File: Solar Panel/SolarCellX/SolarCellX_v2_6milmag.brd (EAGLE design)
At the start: 100 x 82 mm, 17 parts

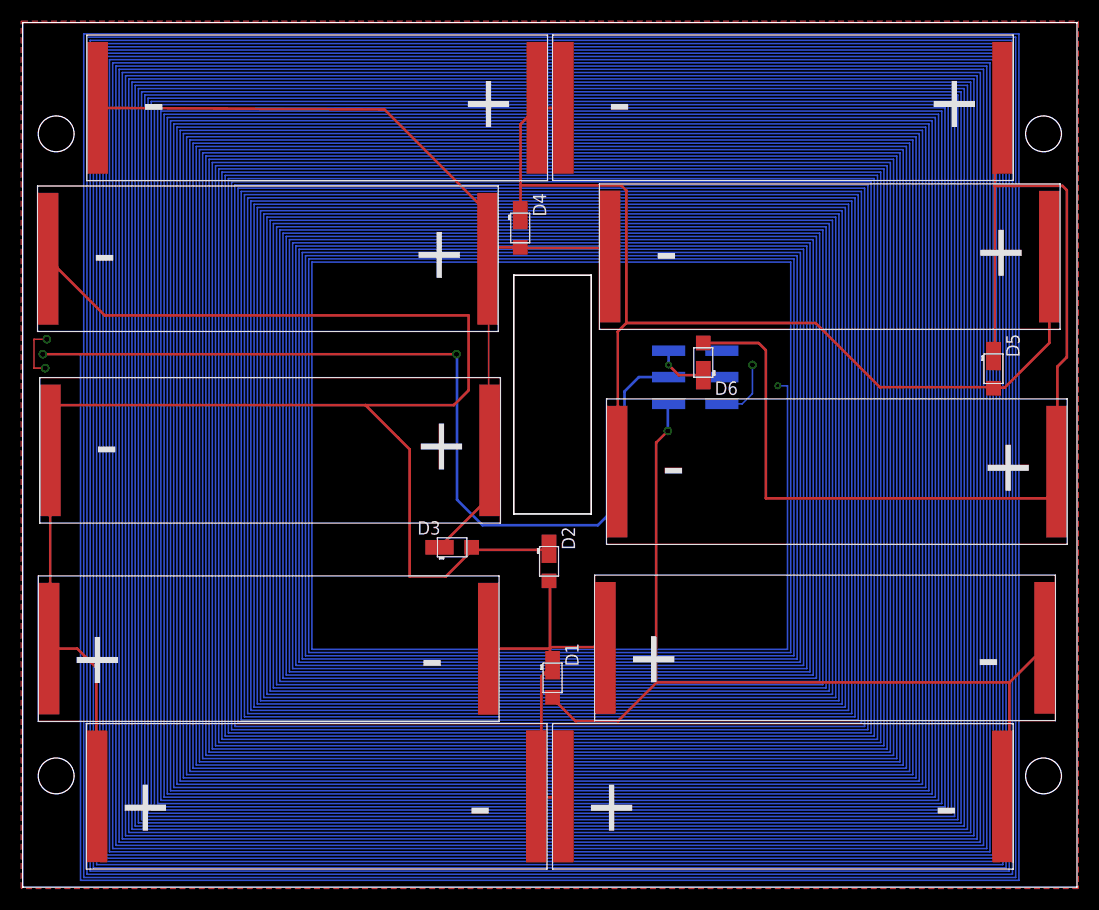
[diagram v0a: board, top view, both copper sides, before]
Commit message: Clearance fixes for X plus gerber generation
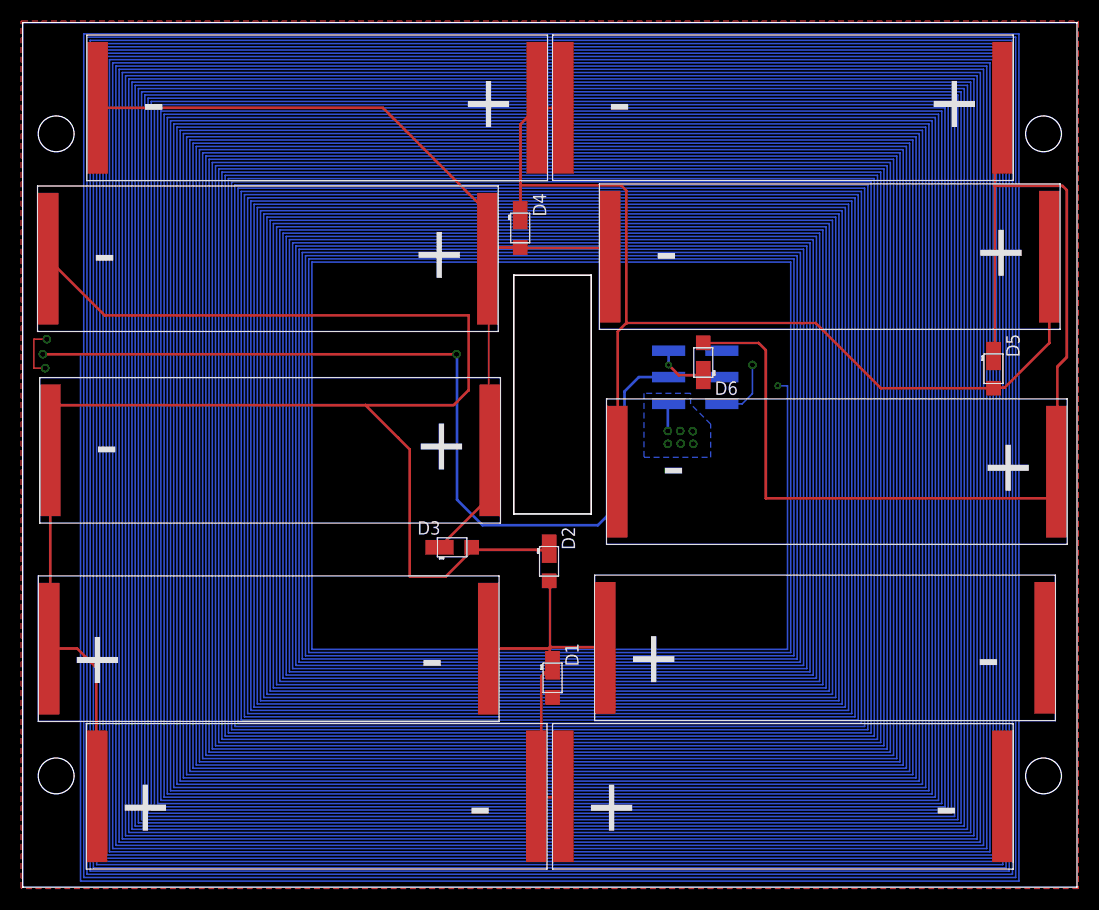
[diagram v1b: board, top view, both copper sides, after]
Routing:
- net GND: track 88.9 -> 2.65 mm, vias 1 -> 6
- added copper zone on layer 16, net GND
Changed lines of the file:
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@@
 <?xml version="1.0" encoding="utf-8"?>
 <!DOCTYPE eagle SYSTEM "eagle.dtd">
-<eagle version="9.3.0">
+<eagle version="9.2.2">
 <drawing>
 <settings>
@@
 <param name="mtCopper" value="0.035559375mm 0.01778125mm 0.0356mm 0.0356mm 0.0356mm 0.0356mm 0.0356mm 0.0356mm 0.0356mm 0.0356mm 0.0356mm 0.0356mm 0.0356mm 0.0356mm 0.01778125mm 0.035559375mm"/>
 <param name="mtIsolate" value="0.17018125mm 47mil 0.2007mm 0.1499mm 0.2007mm 0.1499mm 0.2007mm 0.1499mm 0.2007mm 0.1499mm 0.2007mm 0.1499mm 0.2007mm 0.1499mm 0.17018125mm"/>
-<param name="mdWireWire" value="5mil"/>
-<param name="mdWirePad" value="5mil"/>
-<param name="mdWireVia" value="5mil"/>
-<param name="mdPadPad" value="5mil"/>
-<param name="mdPadVia" value="5mil"/>
-<param name="mdViaVia" value="5mil"/>
-<param name="mdSmdPad" value="5mil"/>
-<param name="mdSmdVia" value="5mil"/>
-<param name="mdSmdSmd" value="5mil"/>
+<param name="mdWireWire" value="7mil"/>
+<param name="mdWirePad" value="7mil"/>
+<param name="mdWireVia" value="7mil"/>
+<param name="mdPadPad" value="7mil"/>
+<param name="mdPadVia" value="7mil"/>
+<param name="mdViaVia" value="7mil"/>
+<param name="mdSmdPad" value="6mil"/>
+<param name="mdSmdVia" value="6mil"/>
+<param name="mdSmdSmd" value="6mil"/>
 <param name="mdViaViaSameLayer" value="8mil"/>
 <param name="mnLayersViaInSmd" value="2"/>
@@
 <wire x1="61.191140625" y1="45.839" x2="61.191140625" y2="43.26381875" width="0.254" layer="16"/>
 <via x="61.191140625" y="43.26381875" extent="1-16" drill="0.5"/>
-<wire x1="61.191140625" y1="43.26381875" x2="60.0837" y2="42.156378125" width="0.254" layer="1"/>
-<wire x1="60.0837" y1="42.156378125" x2="60.0837" y2="19.4183" width="0.254" layer="1"/>
-<wire x1="52.4256" y1="15.748" x2="56.4642" y2="15.748" width="0.254" layer="1"/>
-<wire x1="50.292" y1="17.8816" x2="52.4256" y2="15.748" width="0.254" layer="1"/>
-<wire x1="50.292" y1="17.8816" x2="50.258" y2="18" width="0.1524" layer="1"/>
-<wire x1="93.599" y1="19.4183" x2="93.599" y2="8.6614" width="0.254" layer="1"/>
-<wire x1="96.8121" y1="22.6314" x2="93.599" y2="19.4183" width="0.254" layer="1"/>
-<wire x1="93.599" y1="8.6614" x2="92.9546" y2="8.61" width="0.1524" layer="1"/>
-<wire x1="96.8121" y1="22.6314" x2="96.949" y2="22.693" width="0.1524" layer="1"/>
-<wire x1="93.599" y1="19.4183" x2="60.1345" y2="19.4183" width="0.254" layer="1"/>
-<wire x1="56.4642" y1="15.748" x2="60.1345" y2="19.4183" width="0.254" layer="1"/>
 <polygon width="0" layer="1">
 <vertex x="-0.0508" y="82.1436"/>
@@
 <vertex x="-0.1524" y="82.1436"/>
 </polygon>
+<via x="62.359540625" y="43.26381875" extent="1-16" drill="0.5"/>
+<via x="63.553340625" y="43.23841875" extent="1-16" drill="0.5"/>
+<via x="61.191140625" y="42.04461875" extent="1-16" drill="0.5"/>
+<via x="62.410340625" y="42.07001875" extent="1-16" drill="0.5"/>
+<via x="63.604140625" y="42.04461875" extent="1-16" drill="0.5"/>
+<polygon width="0.1524" layer="16">
+<vertex x="58.928" y="46.8376"/>
+<vertex x="58.928" y="40.767"/>
+<vertex x="65.2526" y="40.767"/>
+<vertex x="65.2526" y="43.9166"/>
+<vertex x="63.3476" y="45.8216"/>
+<vertex x="63.3476" y="46.8376"/>
+</polygon>
 </signal>
 <signal name="N$2">
@@
 <wire x1="51.689" y1="73.9013" x2="51.26" y2="73.92" width="0.1524" layer="1"/>
 <wire x1="48.6156" y1="73.7616" x2="48.7796" y2="73.9114" width="0.1524" layer="1"/>
-<wire x1="75.2178" y1="53.5051" x2="81.3044" y2="47.4185" width="0.254" layer="1"/>
-<wire x1="57.2516" y1="53.5051" x2="75.2178" y2="53.5051" width="0.254" layer="1"/>
-<wire x1="81.3044" y1="47.4185" x2="91.9855" y2="47.4185" width="0.254" layer="1"/>
-<wire x1="91.9855" y1="47.4185" x2="92.083" y2="47.321" width="0.254" layer="1"/>
-<wire x1="93.1291" y1="47.371" x2="92.2528" y2="47.371" width="0.254" layer="1"/>
+<wire x1="75.2178" y1="53.5051" x2="57.2516" y2="53.5051" width="0.254" layer="1"/>
+<wire x1="92.033" y1="47.371" x2="92.083" y2="47.321" width="0.254" layer="1"/>
 <wire x1="97.3709" y1="51.6128" x2="93.1291" y2="47.371" width="0.254" layer="1"/>
-<wire x1="92.083" y1="47.321" x2="92.2528" y2="47.371" width="0" layer="19" extent="1-1"/>
+<wire x1="93.1291" y1="47.371" x2="92.033" y2="47.371" width="0.254" layer="1"/>
+<wire x1="92.083" y1="47.321" x2="81.4019" y2="47.321" width="0.254" layer="1"/>
+<wire x1="81.4019" y1="47.321" x2="75.2178" y2="53.5051" width="0.254" layer="1"/>
 </signal>
 <signal name="N$5">
@@
 <wire x1="44.196" y1="41.3512" x2="44.1452" y2="41.3512" width="0.1524" layer="1"/>
 <wire x1="44.1452" y1="41.3512" x2="44.313" y2="41.428" width="0.1524" layer="1"/>
-<wire x1="7.0796" y1="73.9114" x2="34.318" y2="73.759" width="0.254" layer="1"/>
-<wire x1="44.069" y1="64.008" x2="34.318" y2="73.759" width="0.254" layer="1"/>
 <wire x1="39.529" y1="32.235" x2="43.815" y2="36.521" width="0.254" layer="1"/>
 <wire x1="43.815" y1="36.521" x2="43.815" y2="38.608" width="0.254" layer="1"/>
-<wire x1="44.196" y1="64.008" x2="44.069" y2="64.008" width="0.1524" layer="1"/>
+<wire x1="44.069" y1="64.008" x2="44.196" y2="64.008" width="0.1524" layer="1"/>
 <wire x1="47.19" y1="60.672" x2="44.196" y2="60.672" width="0.254" layer="1"/>
 <wire x1="44.2849" y1="41.3512" x2="44.196" y2="41.3512" width="0.1524" layer="1"/>
@@
 <wire x1="44.313" y1="41.428" x2="43.815" y2="40.93" width="0.1524" layer="1"/>
 <wire x1="43.815" y1="40.93" x2="43.815" y2="38.608" width="0.1524" layer="1"/>
+<wire x1="7.0796" y1="73.9114" x2="34.1656" y2="73.9114" width="0.254" layer="1"/>
+<wire x1="34.1656" y1="73.9114" x2="44.069" y2="64.008" width="0.254" layer="1"/>
 </signal>
 <signal name="V_SOLAR">
@@
 <via x="1.905" y="50.546" extent="1-16" drill="0.5"/>
 <wire x1="1.905" y1="50.546" x2="5.4864" y2="50.546" width="0.1524" layer="16"/>
-<wire x1="5.4864" y1="50.546" x2="5.4864" y2="0.6477" width="0.1524" layer="16"/>
+<wire x1="5.4864" y1="50.546" x2="5.4864" y2="0.5715" width="0.1524" layer="16"/>
 <wire x1="94.488" y1="80.9244" x2="5.7912" y2="80.9244" width="0.1524" layer="16"/>
 <wire x1="5.7912" y1="80.9244" x2="5.7912" y2="0.9144" width="0.1524" layer="16"/>
-<wire x1="5.4864" y1="0.6477" x2="94.488" y2="0.6477" width="0.1524" layer="16"/>
-<wire x1="94.488" y1="0.6477" x2="94.488" y2="80.9244" width="0.1524" layer="16"/>
+<wire x1="5.4864" y1="0.5715" x2="94.488" y2="0.5715" width="0.1524" layer="16"/>
+<wire x1="94.488" y1="0.5715" x2="94.488" y2="80.9244" width="0.1524" layer="16"/>
 <wire x1="5.7912" y1="0.9144" x2="94.1832" y2="0.9144" width="0.1524" layer="16"/>
 <wire x1="94.1832" y1="0.9144" x2="94.1832" y2="80.6196" width="0.1524" layer="16"/>
@@
 <wire x1="1.0668" y1="51.9684" x2="2.286" y2="51.9684" width="0.1524" layer="1"/>
 <wire x1="5.7912" y1="80.9244" x2="94.488" y2="80.9244" width="0.1524" layer="2"/>
-<wire x1="94.488" y1="0.6477" x2="5.4864" y2="0.6477" width="0.1524" layer="2"/>
-<wire x1="94.488" y1="0.6477" x2="94.488" y2="80.9244" width="0.1524" layer="2"/>
+<wire x1="94.488" y1="0.5715" x2="5.4864" y2="0.5715" width="0.1524" layer="2"/>
+<wire x1="94.488" y1="0.5715" x2="94.488" y2="80.9244" width="0.1524" layer="2"/>
 <wire x1="94.1832" y1="0.9144" x2="5.7912" y2="0.9144" width="0.1524" layer="2"/>
 <wire x1="94.1832" y1="0.9144" x2="94.1832" y2="80.6196" width="0.1524" layer="2"/>
@@
 <wire x1="27.1272" y1="22.2504" x2="72.8472" y2="22.2504" width="0.1524" layer="2"/>
 <wire x1="27.432" y1="22.5552" x2="72.5424" y2="22.5552" width="0.1524" layer="2"/>
-<wire x1="5.4864" y1="0.6477" x2="5.4864" y2="51.9684" width="0.1524" layer="2"/>
+<wire x1="5.4864" y1="0.5715" x2="5.4864" y2="51.9684" width="0.1524" layer="2"/>
 <wire x1="72.5424" y1="53.0264" x2="71.628" y2="53.0264" width="0.1524" layer="2"/>
 <wire x1="72.5424" y1="22.5552" x2="72.5424" y2="53.0264" width="0.1524" layer="2"/>
